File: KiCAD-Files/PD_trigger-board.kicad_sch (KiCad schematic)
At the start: 16 parts, among them J1 USB_C_Receptacle_USB3.0_12P, U1 HUSB238, U2 SIR1309DP, U3 ESP32-S3-mini_pinprofile

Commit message: minor changes
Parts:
- U2: footprint blinkyparts:SO_ADY-T1-GE3_VIS -> Package_SO:PowerPAK_SO-8L_Single
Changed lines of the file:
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@@
 			)
 		)
-		(property "Footprint" "blinkyparts:SO_ADY-T1-GE3_VIS"
+		(property "Footprint" "Package_SO:PowerPAK_SO-8L_Single"
 			(at 226.06 40.64 0)
 			(effects

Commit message: added zener and tvs diode
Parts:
- added D1: D_Zener, symbol Device:D_Zener
- added D2: SD15_SOD323, Diode_SMD:D_SOD-323, symbol Diode:SD15_SOD323
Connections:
- net GND: now also D2.1 (A1)
- net VBUS: now also D1.1 (K), D2.2 (A2)
- net at R3.2, R4.1, U2.4 (G): now also D1.2 (A)

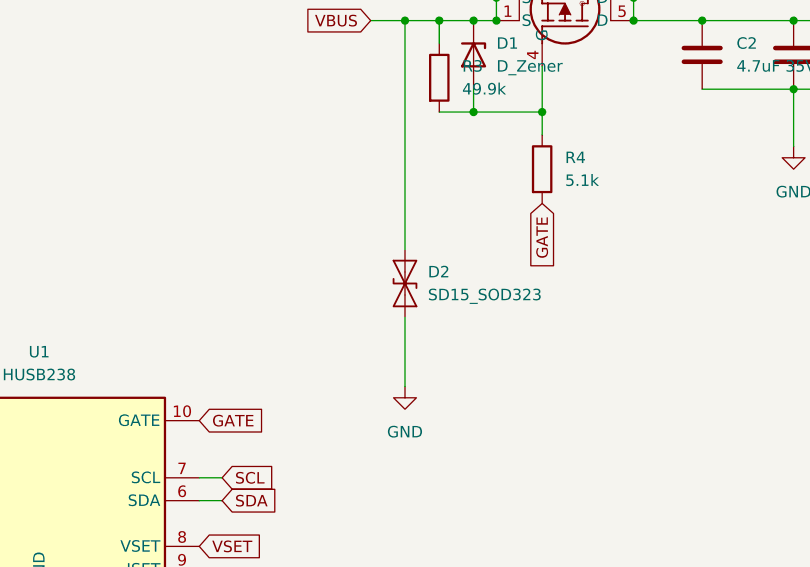
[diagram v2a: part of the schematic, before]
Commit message: placed diodes and minor design changes
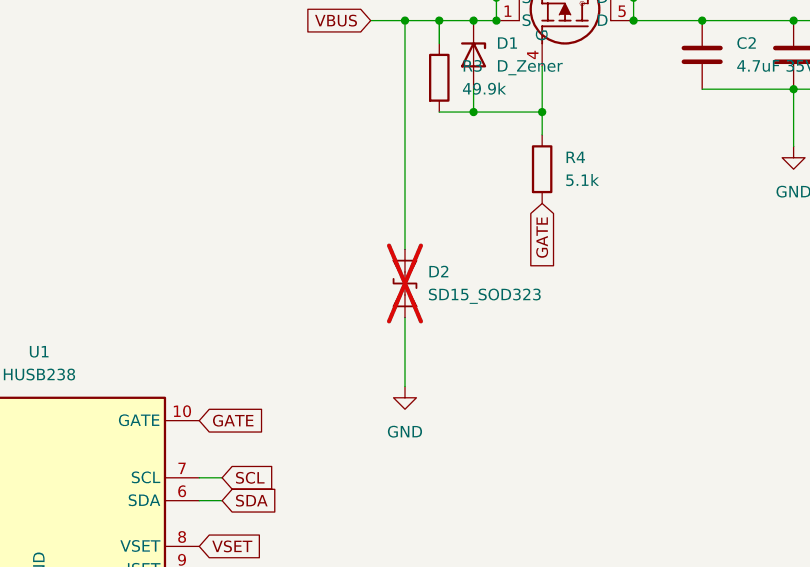
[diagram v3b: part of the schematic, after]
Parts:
- D1: footprint (none) -> Diode_SMD:D_SOD-323; LCSC (none) -> C19077451
- D2: footprint Diode_SMD:D_SOD-323 -> Diode_SMD:D_SOD-323_HandSoldering; LCSC (none) -> C5253553; now not fitted
- J1: LCSC C136423 -> C2927040
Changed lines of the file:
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@@
 			)
 		)
-		(property "LCSC" "C136423"
+		(property "LCSC" "C2927040"
 			(at 40.64 85.09 0)
 			(effects
@@
 			)
 		)
-		(property "Footprint" ""
+		(property "Footprint" "Diode_SMD:D_SOD-323"
 			(at 218.44 39.37 0)
 			(effects
@@
 			)
 		)
+		(property "LCSC" "C19077451"
+			(at 218.44 39.37 90)
+			(effects
+				(font
+					(size 1.27 1.27)
+				)
+				(hide yes)
+			)
+		)
 		(pin "2"
 		)
@@
 		(in_bom yes)
 		(on_board yes)
-		(dnp no)
+		(dnp yes)
 		(fields_autoplaced yes)
 		(property "Reference" "D2"
@@
 			)
 		)
-		(property "Footprint" "Diode_SMD:D_SOD-323"
+		(property "Footprint" "Diode_SMD:D_SOD-323_HandSoldering"
 			(at 215.9 64.77 0)
 			(effects
@@
 			(effects
 				(font
+					(size 1.27 1.27)
+				)
+				(hide yes)
+			)
+		)
+		(property "LCSC" "C5253553"
+			(at 210.82 64.77 90)
+			(effects
+				(font
